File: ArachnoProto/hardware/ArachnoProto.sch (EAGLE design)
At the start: 26 parts, among them J1 PINHEAD-17-REV, J2 PINHEAD-17-REV

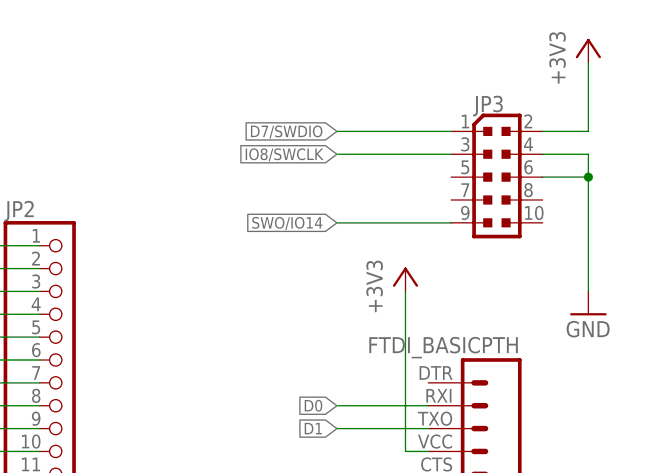
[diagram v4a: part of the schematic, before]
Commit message: Fixed broken debug port
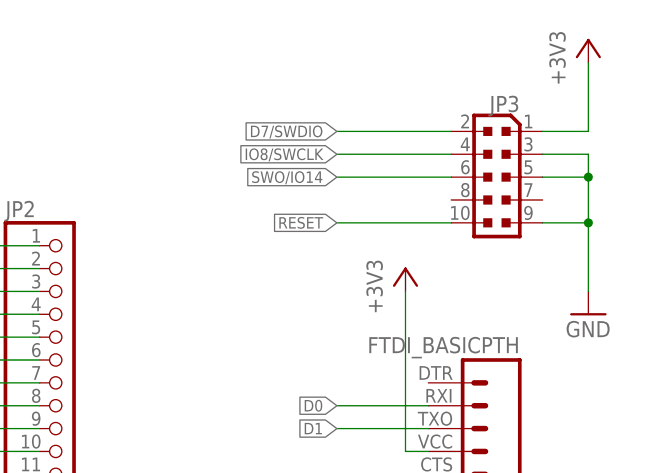
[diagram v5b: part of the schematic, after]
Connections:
- net +3V3: now also JP3.1; no longer JP3.2
- net D7/SWDIO: now also JP3.2; no longer JP3.1
- net GND: now also JP3.3, JP3.5, JP3.9; no longer JP3.4, JP3.6
- net IO8/SWCLK: now also JP3.4; no longer JP3.3
- net RESET: now also JP3.10
- net SWO/IO14: now also JP3.6; no longer JP3.9
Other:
- moved on the sheet: JP3
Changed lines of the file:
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@@
 <instance part="+3V6" gate="G$1" x="251.46" y="185.42"/>
 <instance part="GND8" gate="1" x="251.46" y="154.94"/>
-<instance part="JP3" gate="G$1" x="241.3" y="170.18"/>
+<instance part="JP3" gate="G$1" x="241.3" y="170.18" rot="MR0"/>
 <instance part="JP4" gate="G$1" x="238.76" y="142.24" rot="R180"/>
 <instance part="GND5" gate="1" x="231.14" y="127"/>
@@
 <pinref part="J1" gate="G$1" pin="39"/>
 <junction x="121.92" y="152.4"/>
+</segment>
+<segment>
+<pinref part="JP3" gate="G$1" pin="10"/>
+<wire x1="236.22" y1="165.1" x2="223.52" y2="165.1" width="0.1524" layer="91"/>
+<label x="223.52" y="165.1" size="1.27" layer="95" rot="R180" xref="yes"/>
 </segment>
 </net>
@@
 <segment>
 <pinref part="GND8" gate="1" pin="GND"/>
-<wire x1="251.46" y1="157.48" x2="251.46" y2="170.18" width="0.1524" layer="91"/>
+<wire x1="251.46" y1="157.48" x2="251.46" y2="165.1" width="0.1524" layer="91"/>
+<pinref part="JP3" gate="G$1" pin="9"/>
+<wire x1="251.46" y1="165.1" x2="251.46" y2="170.18" width="0.1524" layer="91"/>
+<wire x1="251.46" y1="170.18" x2="251.46" y2="172.72" width="0.1524" layer="91"/>
+<wire x1="246.38" y1="165.1" x2="251.46" y2="165.1" width="0.1524" layer="91"/>
+<pinref part="JP3" gate="G$1" pin="3"/>
 <wire x1="246.38" y1="172.72" x2="251.46" y2="172.72" width="0.1524" layer="91"/>
-<wire x1="251.46" y1="172.72" x2="251.46" y2="170.18" width="0.1524" layer="91"/>
+<pinref part="JP3" gate="G$1" pin="5"/>
 <wire x1="246.38" y1="170.18" x2="251.46" y2="170.18" width="0.1524" layer="91"/>
 <junction x="251.46" y="170.18"/>
-<pinref part="JP3" gate="G$1" pin="4"/>
-<pinref part="JP3" gate="G$1" pin="6"/>
+<junction x="251.46" y="165.1"/>
 </segment>
 <segment>
@@
 <wire x1="236.22" y1="172.72" x2="223.52" y2="172.72" width="0.1524" layer="91"/>
 <label x="223.52" y="172.72" size="1.27" layer="95" rot="R180" xref="yes"/>
-<pinref part="JP3" gate="G$1" pin="3"/>
+<pinref part="JP3" gate="G$1" pin="4"/>
 </segment>
 </net>
@@
 <wire x1="236.22" y1="175.26" x2="223.52" y2="175.26" width="0.1524" layer="91"/>
 <label x="223.52" y="175.26" size="1.27" layer="95" rot="R180" xref="yes"/>
-<pinref part="JP3" gate="G$1" pin="1"/>
+<pinref part="JP3" gate="G$1" pin="2"/>
 </segment>
 </net>
@@
 </segment>
 <segment>
-<wire x1="236.22" y1="165.1" x2="223.52" y2="165.1" width="0.1524" layer="91"/>
-<label x="223.52" y="165.1" size="1.27" layer="95" rot="R180" xref="yes"/>
-<pinref part="JP3" gate="G$1" pin="9"/>
+<wire x1="236.22" y1="170.18" x2="223.52" y2="170.18" width="0.1524" layer="91"/>
+<label x="223.52" y="170.18" size="1.27" layer="95" rot="R180" xref="yes"/>
+<pinref part="JP3" gate="G$1" pin="6"/>
 </segment>
 </net>
@@
 <pinref part="+3V6" gate="G$1" pin="+3V3"/>
 <wire x1="251.46" y1="182.88" x2="251.46" y2="175.26" width="0.1524" layer="91"/>
+<pinref part="JP3" gate="G$1" pin="1"/>
 <wire x1="251.46" y1="175.26" x2="246.38" y2="175.26" width="0.1524" layer="91"/>
-<pinref part="JP3" gate="G$1" pin="2"/>
-</segment>
-<segment>
+</segment>
+<segment>
